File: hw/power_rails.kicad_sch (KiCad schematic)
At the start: 15 parts, among them U2 TPS2116DRLR, U3 TPS563201DDCR

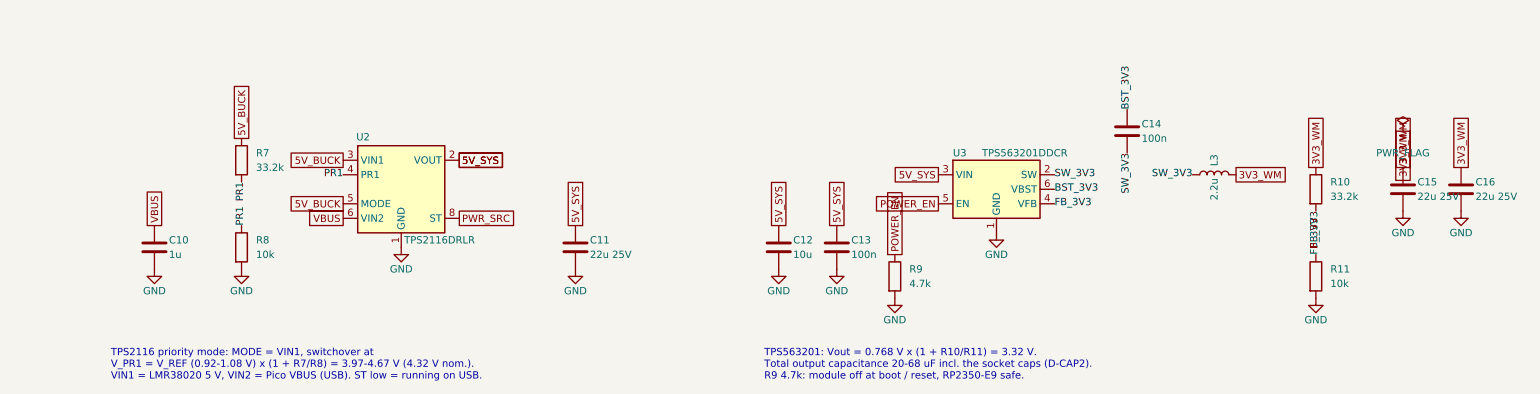
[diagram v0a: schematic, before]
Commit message: hw: draw schematic with wires instead of net labels
Connections inside a sheet are now wires; global labels remain only for
nets that cross sheets, GND stays on power symbols. Pico pins 9-20 are
fanned out so the 33R series resistors fit in one column, and the
SX1302_RESET pull-down moves to the LoRa sheet. Netlist unchanged, ERC
clean. Project file now carries KiCad's default settings.

Co-Authored-By: Claude Opus 5.5 <noreply@anthropic.com>
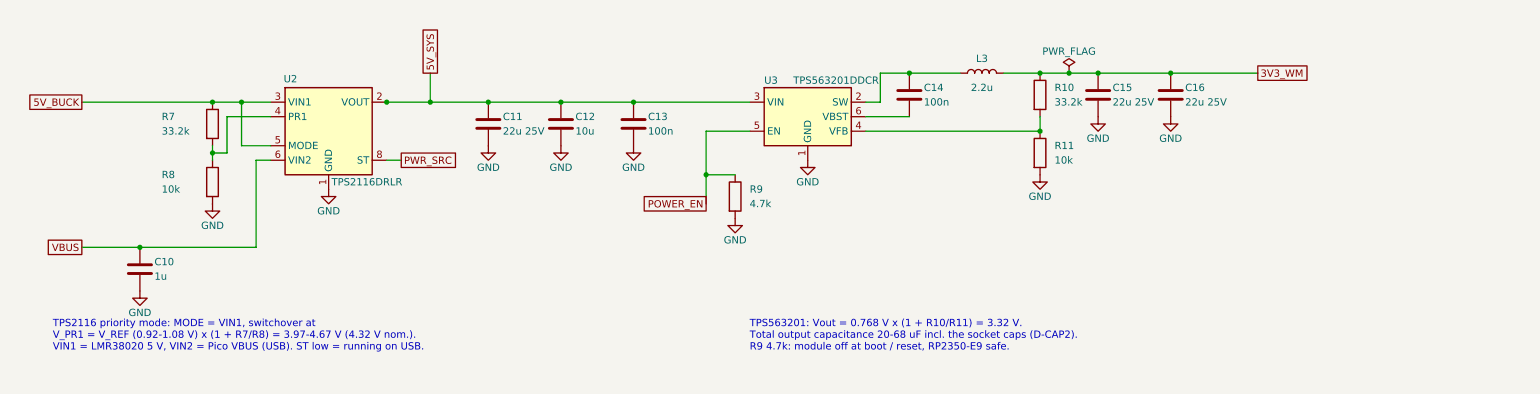
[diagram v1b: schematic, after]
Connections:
- net BST_3V3: no longer names the net of C14.1
- net BST_3V3: now also L3.1, U3.2 (SW); no longer U3.6 (VBST)
- net FB_3V3: no longer names the net of R10.2, R11.1, U3.4 (VFB)
- net PR1: no longer names the net of R7.2, R8.1, U2.4 (PR1)
- removed net SW_3V3: C14.2, L3.1, U3.2 (SW)
- new net: C14.2, U3.6 (VBST)
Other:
- moved on the sheet: C10, C11, C12, C13, C14, C15, C16, L3, R10, R11, R7, R8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
